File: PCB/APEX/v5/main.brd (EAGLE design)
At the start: 38.1 x 38.1 mm, 4 parts

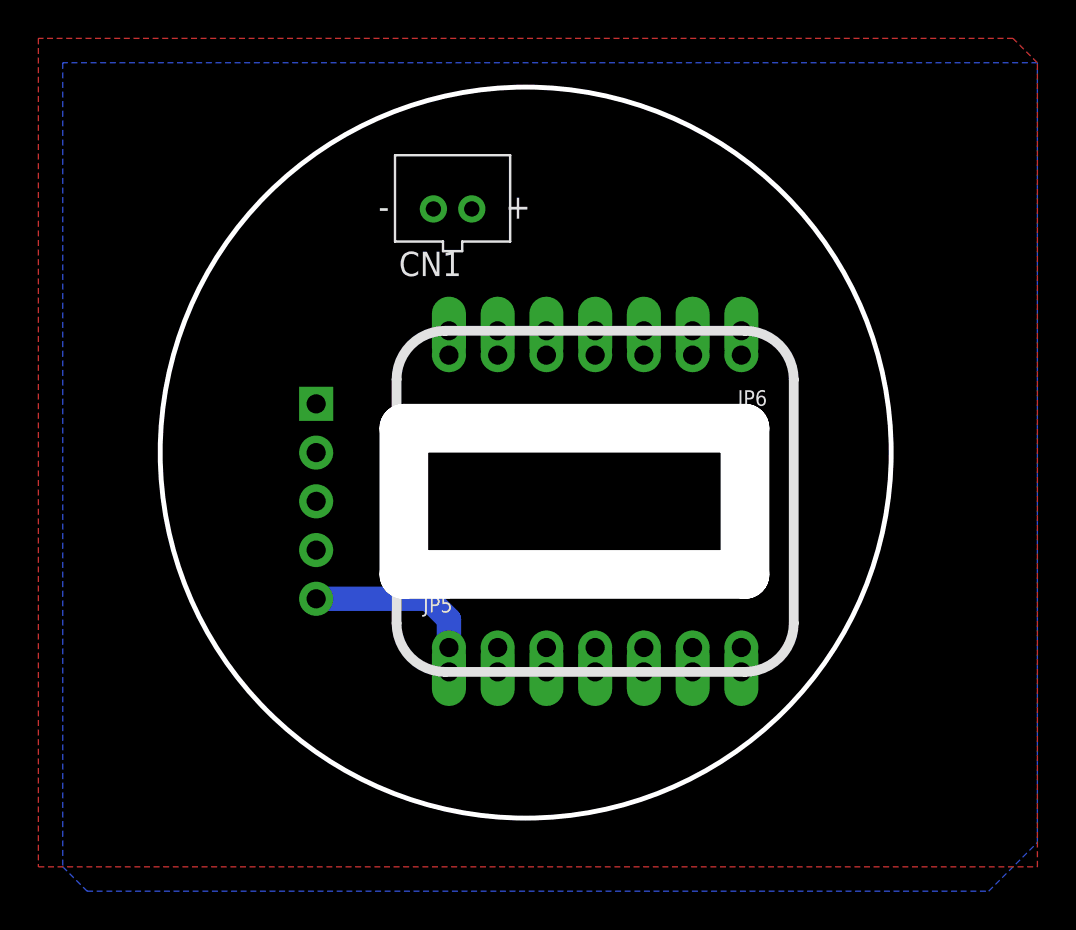
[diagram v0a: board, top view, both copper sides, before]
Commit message: move boards inside slightly
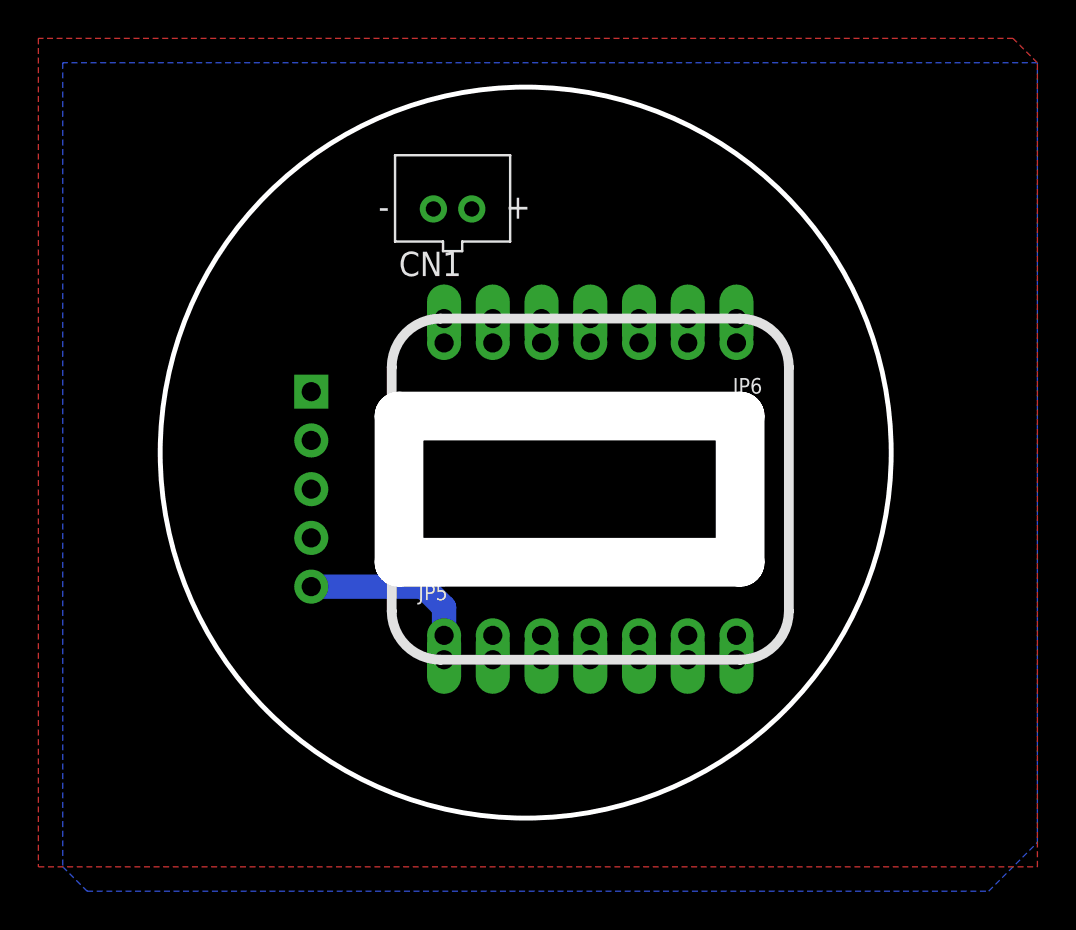
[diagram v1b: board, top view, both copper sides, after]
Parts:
- moved JP2 0.68 mm to (54.9, 109.9)
- moved JP5 0.68 mm to (69.4, 102.2)
- moved JP6 0.68 mm to (69.4, 117.5)
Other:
- outline, holes or cut-outs redrawn
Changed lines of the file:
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@@
 <board>
 <plain>
-<wire x1="52.07" y1="114.3" x2="52.07" y2="104.14" width="0.508" layer="22"/>
-<wire x1="52.07" y1="104.14" x2="54.61" y2="101.6" width="0.508" layer="22" curve="90"/>
-<wire x1="54.61" y1="101.6" x2="73.66" y2="101.6" width="0.508" layer="22"/>
-<wire x1="73.66" y1="101.6" x2="76.2" y2="104.14" width="0.508" layer="22" curve="90"/>
-<wire x1="76.2" y1="104.14" x2="76.2" y2="114.3" width="0.508" layer="22"/>
-<wire x1="76.2" y1="114.3" x2="73.66" y2="116.84" width="0.508" layer="22" curve="90"/>
-<wire x1="73.66" y1="116.84" x2="54.61" y2="116.84" width="0.508" layer="22"/>
-<wire x1="54.61" y1="116.84" x2="52.07" y2="114.3" width="0.508" layer="22" curve="90"/>
-<wire x1="61.849" y1="118.11" x2="77.47" y2="118.11" width="0.508" layer="21"/>
-<wire x1="77.47" y1="118.11" x2="80.01" y2="115.57" width="0.508" layer="21" curve="-90"/>
-<wire x1="80.01" y1="115.57" x2="80.01" y2="102.87" width="0.508" layer="21"/>
-<wire x1="80.01" y1="102.87" x2="77.47" y2="100.33" width="0.508" layer="21" curve="-90"/>
-<wire x1="77.47" y1="100.33" x2="61.849" y2="100.33" width="0.508" layer="21"/>
-<wire x1="61.849" y1="100.33" x2="59.309" y2="102.87" width="0.508" layer="21" curve="-90"/>
-<wire x1="59.309" y1="102.87" x2="59.309" y2="115.57" width="0.508" layer="21"/>
-<wire x1="59.309" y1="115.57" x2="61.849" y2="118.11" width="0.508" layer="21" curve="-90"/>
+<wire x1="51.816" y1="114.935" x2="51.816" y2="104.775" width="0.508" layer="22"/>
+<wire x1="51.816" y1="104.775" x2="54.356" y2="102.235" width="0.508" layer="22" curve="90"/>
+<wire x1="54.356" y1="102.235" x2="73.406" y2="102.235" width="0.508" layer="22"/>
+<wire x1="73.406" y1="102.235" x2="75.946" y2="104.775" width="0.508" layer="22" curve="90"/>
+<wire x1="75.946" y1="104.775" x2="75.946" y2="114.935" width="0.508" layer="22"/>
+<wire x1="75.946" y1="114.935" x2="73.406" y2="117.475" width="0.508" layer="22" curve="90"/>
+<wire x1="73.406" y1="117.475" x2="54.356" y2="117.475" width="0.508" layer="22"/>
+<wire x1="54.356" y1="117.475" x2="51.816" y2="114.935" width="0.508" layer="22" curve="90"/>
+<wire x1="61.595" y1="118.745" x2="77.216" y2="118.745" width="0.508" layer="21"/>
+<wire x1="77.216" y1="118.745" x2="79.756" y2="116.205" width="0.508" layer="21" curve="-90"/>
+<wire x1="79.756" y1="116.205" x2="79.756" y2="103.505" width="0.508" layer="21"/>
+<wire x1="79.756" y1="103.505" x2="77.216" y2="100.965" width="0.508" layer="21" curve="-90"/>
+<wire x1="77.216" y1="100.965" x2="61.595" y2="100.965" width="0.508" layer="21"/>
+<wire x1="61.595" y1="100.965" x2="59.055" y2="103.505" width="0.508" layer="21" curve="-90"/>
+<wire x1="59.055" y1="103.505" x2="59.055" y2="116.205" width="0.508" layer="21"/>
+<wire x1="59.055" y1="116.205" x2="61.595" y2="118.745" width="0.508" layer="21" curve="-90"/>
 <text x="115.2398" y="58.4708" size="1.016" layer="21" font="vector" ratio="12" rot="R180" align="center"></text>
 <circle x="66.04" y="111.76" radius="19.05" width="0.254" layer="20"/>
-<wire x1="59.69" y1="113.03" x2="77.47" y2="113.03" width="2.54" layer="46"/>
-<wire x1="77.47" y1="113.03" x2="77.47" y2="105.41" width="2.54" layer="46"/>
-<wire x1="77.47" y1="105.41" x2="59.69" y2="105.41" width="2.54" layer="46"/>
-<wire x1="59.69" y1="105.41" x2="59.69" y2="113.03" width="2.54" layer="46"/>
+<wire x1="59.436" y1="113.665" x2="77.216" y2="113.665" width="2.54" layer="46"/>
+<wire x1="77.216" y1="113.665" x2="77.216" y2="106.045" width="2.54" layer="46"/>
+<wire x1="77.216" y1="106.045" x2="59.436" y2="106.045" width="2.54" layer="46"/>
+<wire x1="59.436" y1="106.045" x2="59.436" y2="113.665" width="2.54" layer="46"/>
 </plain>
 <attributes>
@@
 </autorouter>
 <elements>
-<element name="JP2" library="microbuilder" package="1X05_ROUND_70" value="" x="55.118" y="109.22" smashed="yes" rot="MR270">
-<attribute name="VALUE" x="57.023" y="115.57" size="0.4064" layer="28" ratio="10" rot="MR270"/>
+<element name="JP2" library="microbuilder" package="1X05_ROUND_70" value="" x="54.864" y="109.855" smashed="yes" rot="MR270">
+<attribute name="VALUE" x="56.769" y="116.205" size="0.4064" layer="28" ratio="10" rot="MR270"/>
 </element>
-<element name="JP5" library="microbuilder" package="1X07_CASTEL" value="" x="69.6595" y="101.6" smashed="yes">
-<attribute name="NAME" x="60.6933" y="103.4288" size="0.8128" layer="25" ratio="18"/>
-<attribute name="VALUE" x="60.7695" y="98.425" size="0.4064" layer="27" ratio="10"/>
+<element name="JP5" library="microbuilder" package="1X07_CASTEL" value="" x="69.4055" y="102.235" smashed="yes">
+<attribute name="NAME" x="60.4393" y="104.0638" size="0.8128" layer="25" ratio="18"/>
+<attribute name="VALUE" x="60.5155" y="99.06" size="0.4064" layer="27" ratio="10"/>
 </element>
-<element name="JP6" library="microbuilder" package="1X07_CASTEL" value="" x="69.6595" y="116.84" smashed="yes" rot="R180">
-<attribute name="NAME" x="78.6257" y="115.0112" size="0.8128" layer="25" ratio="18" rot="R180"/>
-<attribute name="VALUE" x="78.5495" y="120.015" size="0.4064" layer="27" ratio="10" rot="R180"/>
+<element name="JP6" library="microbuilder" package="1X07_CASTEL" value="" x="69.4055" y="117.475" smashed="yes" rot="R180">
+<attribute name="NAME" x="78.3717" y="115.6462" size="0.8128" layer="25" ratio="18" rot="R180"/>
+<attribute name="VALUE" x="78.2955" y="120.65" size="0.4064" layer="27" ratio="10" rot="R180"/>
 </element>
 <element name="CN1" library="adafruit" package="JST-PH-2-THM" value="" x="62.23" y="124.46" smashed="yes">
@@
 <contactref element="JP5" pad="1C"/>
 <contactref element="JP2" pad="5"/>
-<wire x1="55.118" y1="104.14" x2="60.96" y2="104.14" width="1.27" layer="16"/>
-<wire x1="60.96" y1="104.14" x2="62.0395" y2="103.0605" width="1.27" layer="16"/>
-<wire x1="62.0395" y1="103.0605" x2="62.0395" y2="100.33" width="1.27" layer="16"/>
-<wire x1="62.0395" y1="100.33" x2="62.0395" y2="101.6" width="0" layer="19" extent="1-1"/>
+<wire x1="54.864" y1="104.775" x2="60.706" y2="104.775" width="1.27" layer="16"/>
+<wire x1="60.706" y1="104.775" x2="61.7855" y2="103.6955" width="1.27" layer="16"/>
+<wire x1="61.7855" y1="103.6955" x2="61.7855" y2="100.965" width="1.27" layer="16"/>
+<wire x1="61.7855" y1="100.965" x2="61.7855" y2="102.235" width="0" layer="19" extent="1-1"/>
 </signal>
 <signal name="A1">
 <contactref element="JP5" pad="2"/>
 <contactref element="JP5" pad="2C"/>
-<wire x1="64.5795" y1="100.33" x2="64.5795" y2="101.6" width="0" layer="19" extent="1-1"/>
+<wire x1="64.3255" y1="100.965" x2="64.3255" y2="102.235" width="0" layer="19" extent="1-1"/>
 </signal>
 <signal name="MOSI">
 <contactref element="JP6" pad="4"/>
 <contactref element="JP6" pad="4C"/>
-<wire x1="69.6595" y1="118.11" x2="69.6595" y2="116.84" width="0" layer="19" extent="1-1"/>
+<wire x1="69.4055" y1="118.745" x2="69.4055" y2="117.475" width="0" layer="19" extent="1-1"/>
 </signal>
 <signal name="MISO">
 <contactref element="JP6" pad="3"/>
 <contactref element="JP6" pad="3C"/>
-<wire x1="72.1995" y1="118.11" x2="72.1995" y2="116.84" width="0" layer="19" extent="1-1"/>
+<wire x1="71.9455" y1="118.745" x2="71.9455" y2="117.475" width="0" layer="19" extent="1-1"/>
 </signal>
 <signal name="SCK">
 <contactref element="JP6" pad="2"/>
 <contactref element="JP6" pad="2C"/>
-<wire x1="74.7395" y1="118.11" x2="74.7395" y2="116.84" width="0" layer="19" extent="1-1"/>
+<wire x1="74.4855" y1="118.745" x2="74.4855" y2="117.475" width="0" layer="19" extent="1-1"/>
 </signal>
 <signal name="A2">
 <contactref element="JP5" pad="3"/>
 <contactref element="JP5" pad="3C"/>
-<wire x1="67.1195" y1="100.33" x2="67.1195" y2="101.6" width="0" layer="19" extent="1-1"/>
+<wire x1="66.8655" y1="100.965" x2="66.8655" y2="102.235" width="0" layer="19" extent="1-1"/>
 </signal>
 <signal name="A3">
 <contactref element="JP5" pad="4"/>
 <contactref element="JP5" pad="4C"/>
-<wire x1="69.6595" y1="100.33" x2="69.6595" y2="101.6" width="0" layer="19" extent="1-1"/>
+<wire x1="69.4055" y1="100.965" x2="69.4055" y2="102.235" width="0" layer="19" extent="1-1"/>
 </signal>
 <signal name="SDA">
 <contactref element="JP5" pad="5"/>
 <contactref element="JP5" pad="5C"/>
-<wire x1="72.1995" y1="100.33" x2="72.1995" y2="101.6" width="0" layer="19" extent="1-1"/>
+<wire x1="71.9455" y1="100.965" x2="71.9455" y2="102.235" width="0" layer="19" extent="1-1"/>
 </signal>
 <signal name="SCL">
 <contactref element="JP5" pad="6"/>
 <contactref element="JP5" pad="6C"/>
-<wire x1="74.7395" y1="100.33" x2="74.7395" y2="101.6" width="0" layer="19" extent="1-1"/>
+<wire x1="74.4855" y1="100.965" x2="74.4855" y2="102.235" width="0" layer="19" extent="1-1"/>
 </signal>
 <signal name="+3V3">
 <contactref element="JP6" pad="5"/>
 <contactref element="JP6" pad="5C"/>
-<wire x1="67.1195" y1="118.11" x2="67.1195" y2="116.84" width="0" layer="19" extent="1-1"/>
+<wire x1="66.8655" y1="118.745" x2="66.8655" y2="117.475" width="0" layer="19" extent="1-1"/>
 </signal>
 <signal name="PB22/I6/SERCOM5.1">
@@
 <contactref element="JP5" pad="7"/>
 <contactref element="JP5" pad="7C"/>
-<wire x1="77.2795" y1="100.33" x2="77.2795" y2="101.6" width="0" layer="19" extent="1-1"/>
+<wire x1="77.0255" y1="100.965" x2="77.0255" y2="102.235" width="0" layer="19" extent="1-1"/>
 </signal>
 <signal name="RX">
 <contactref element="JP6" pad="1"/>
 <contactref element="JP6" pad="1C"/>
-<wire x1="77.2795" y1="118.11" x2="77.2795" y2="116.84" width="0" layer="19" extent="1-1"/>
+<wire x1="77.0255" y1="118.745" x2="77.0255" y2="117.475" width="0" layer="19" extent="1-1"/>
 </signal>
 </signals>

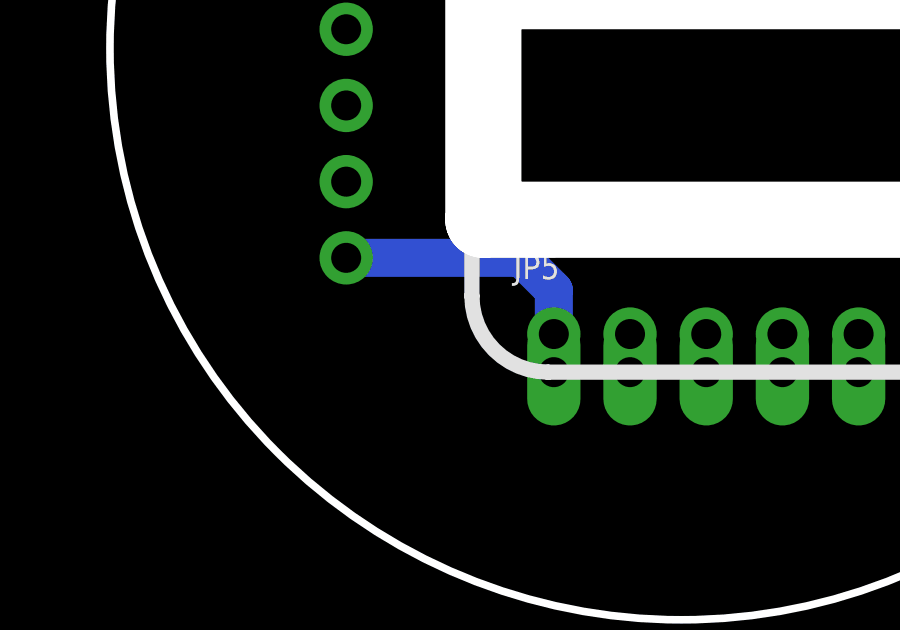
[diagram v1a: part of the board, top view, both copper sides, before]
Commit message: reroute trace around slot
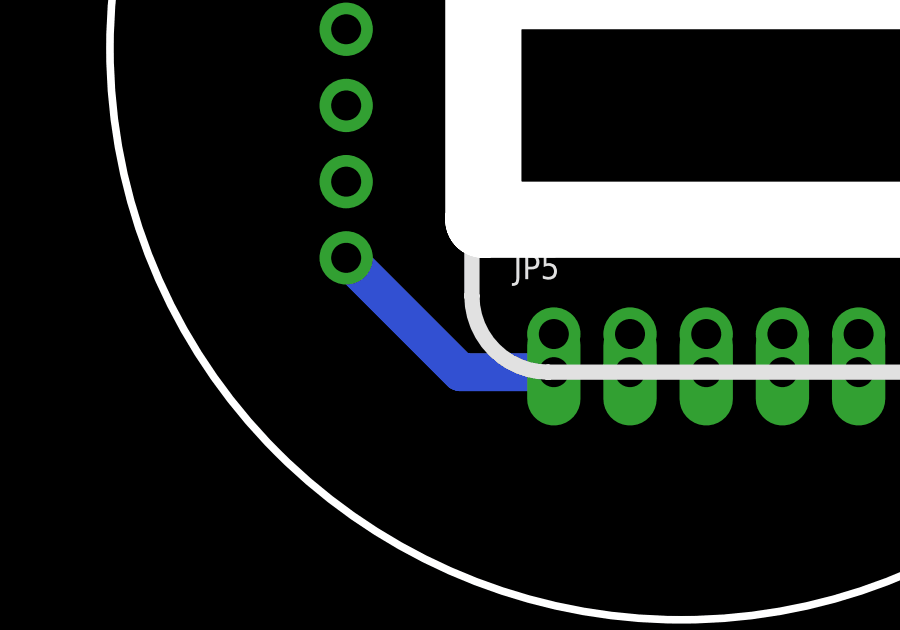
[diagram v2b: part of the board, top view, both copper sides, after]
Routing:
- net AIN+: track 10.1 -> 8.50 mm
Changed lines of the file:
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@@
 <contactref element="JP5" pad="1C"/>
 <contactref element="JP2" pad="5"/>
-<wire x1="54.864" y1="104.775" x2="60.706" y2="104.775" width="1.27" layer="16"/>
-<wire x1="60.706" y1="104.775" x2="61.7855" y2="103.6955" width="1.27" layer="16"/>
-<wire x1="61.7855" y1="103.6955" x2="61.7855" y2="100.965" width="1.27" layer="16"/>
+<wire x1="54.864" y1="104.775" x2="58.674" y2="100.965" width="1.27" layer="16"/>
+<wire x1="61.7855" y1="100.965" x2="58.674" y2="100.965" width="1.27" layer="16"/>
 <wire x1="61.7855" y1="100.965" x2="61.7855" y2="102.235" width="0" layer="19" extent="1-1"/>
 </signal>

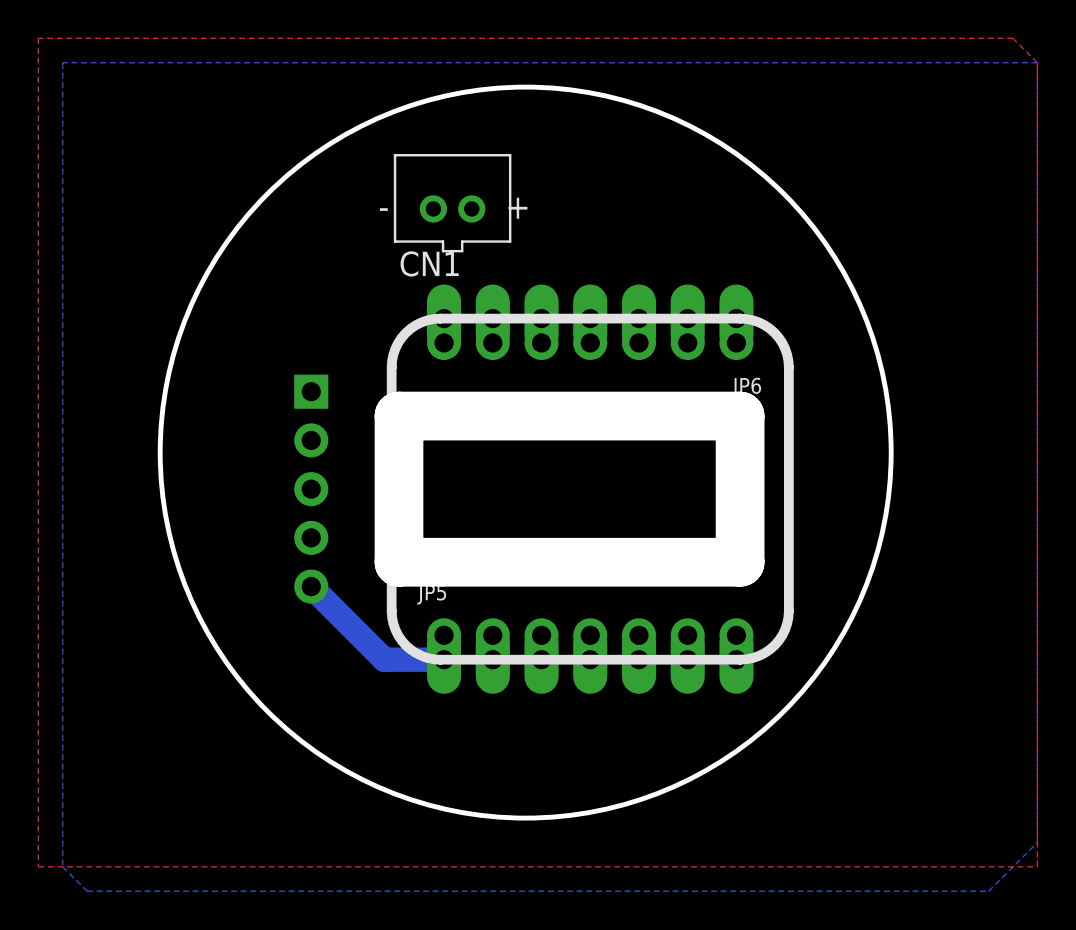
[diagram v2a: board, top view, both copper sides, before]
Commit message: introduce test points, rotate mcu for better usb pos
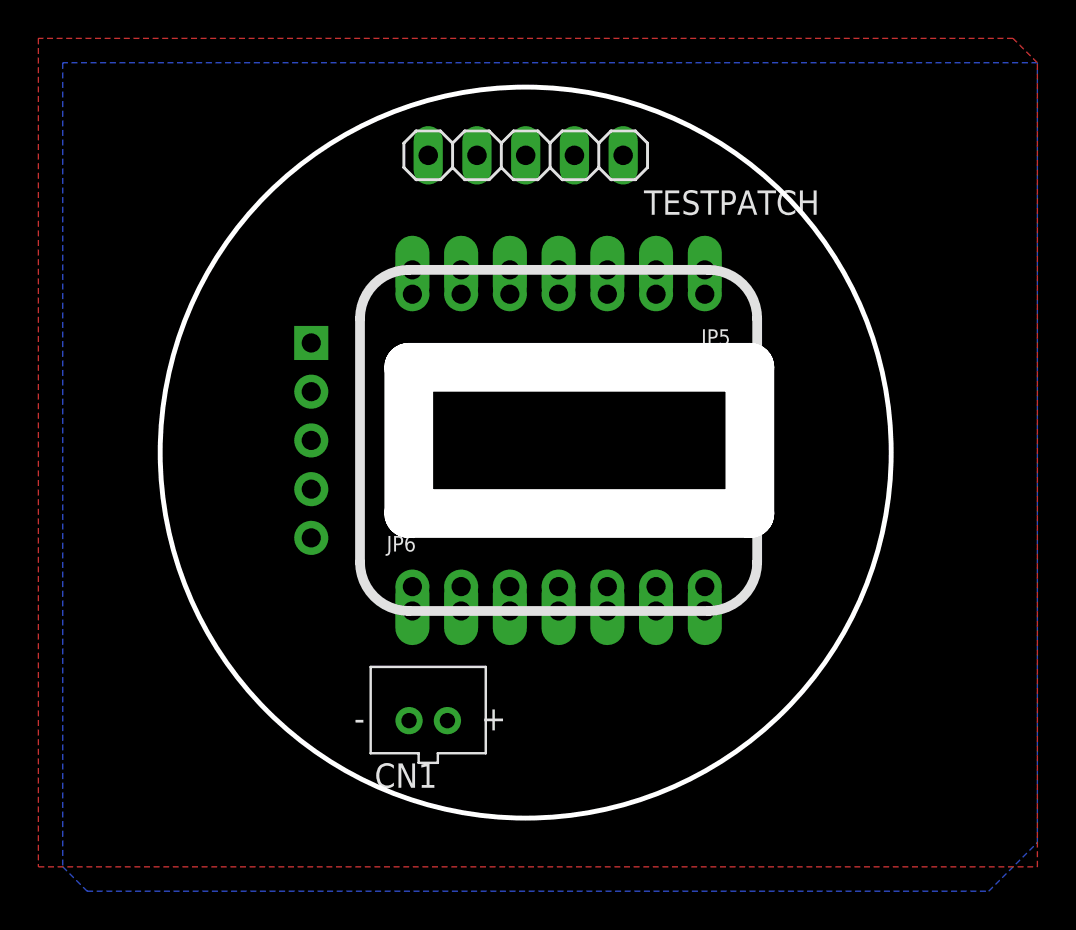
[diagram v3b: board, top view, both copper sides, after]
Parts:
- added TESTPATCH: (no value), pinhead:1X05
- moved CN1 26.7 mm to (61.0, 97.8)
- moved JP5 17.9 mm to (67.8, 120.0), turned to 180 degrees
- moved JP6 12.8 mm to (67.8, 104.8), turned to 0 degrees
- moved JP2 2.54 mm to (54.9, 112.4)
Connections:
- net AIN+: now also TESTPATCH.3
- net GND: now also TESTPATCH.2
- net SCL: now also TESTPATCH.5
- net SDA: now also TESTPATCH.4
- net VCC: now also TESTPATCH.1
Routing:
- net AIN+: track 8.50 -> 0.00 mm
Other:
- outline, holes or cut-outs redrawn
